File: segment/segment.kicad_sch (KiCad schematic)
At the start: 23 parts, among them J1 Voltage Taps In [1-13], J2 Thermistors In [1-12], J3 Thermistors In [13-24], J4 Voltage Taps Out [1-13], J5 Thermistors Out [1-12], J6 Thermistors Out [13-24]

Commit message: feat(segment): add sheet info
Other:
- company: (none) -> SUFST
- title: (none) -> BMS Segment Connector
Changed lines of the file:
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@@
 (kicad_sch (version 20211123) (generator eeschema)
   (paper "A4")
+  (title_block
+    (title "BMS Segment Connector")
+    (date "2022-12-02")
+    (rev "1.0.0")
+    (company "SUFST")
+    (comment 1 "STAG 9")
+    (comment 2 "Tim Brewis")
+  )
   (junction (at 43.815 147.32) (diameter 0) (color 0 0 0 0)
   )

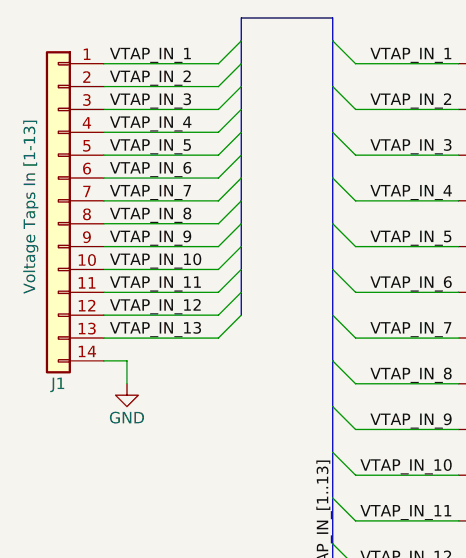
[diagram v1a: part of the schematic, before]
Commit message: feat(segment): re-do layout to reduce board width
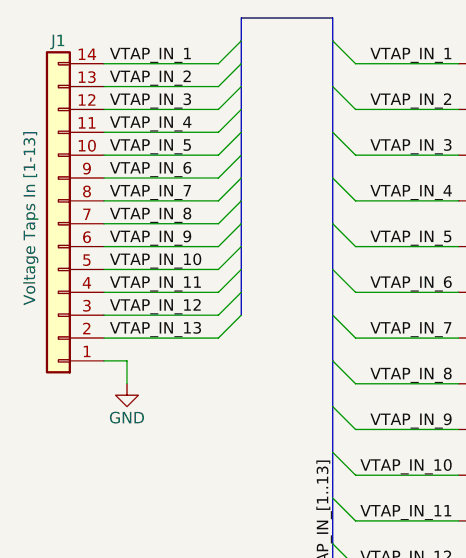
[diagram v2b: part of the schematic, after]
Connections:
- net GND: now also J1.1 (Pin_1); no longer J1.14 (Pin_14)
- net VTAP_IN_1: now also J1.14 (Pin_14); no longer J1.1 (Pin_1)
- net VTAP_IN_10: now also J1.5 (Pin_5); no longer J1.10 (Pin_10)
- net VTAP_IN_11: now also J1.4 (Pin_4); no longer J1.11 (Pin_11)
- net VTAP_IN_12: now also J1.3 (Pin_3); no longer J1.12 (Pin_12)
- net VTAP_IN_13: now also J1.2 (Pin_2); no longer J1.13 (Pin_13)
- net VTAP_IN_2: now also J1.13 (Pin_13); no longer J1.2 (Pin_2)
- net VTAP_IN_3: now also J1.12 (Pin_12); no longer J1.3 (Pin_3)
- net VTAP_IN_4: now also J1.11 (Pin_11); no longer J1.4 (Pin_4)
- net VTAP_IN_5: now also J1.10 (Pin_10); no longer J1.5 (Pin_5)
- net VTAP_IN_6: now also J1.9 (Pin_9); no longer J1.6 (Pin_6)
- net VTAP_IN_7: now also J1.8 (Pin_8); no longer J1.7 (Pin_7)
- net VTAP_IN_8: now also J1.7 (Pin_7); no longer J1.8 (Pin_8)
- net VTAP_IN_9: now also J1.6 (Pin_6); no longer J1.9 (Pin_9)
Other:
- title: BMS Segment Connector -> Segment PCB
- moved on the sheet: J1
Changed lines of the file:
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@@
   (paper "A4")
   (title_block
-    (title "BMS Segment Connector")
-    (date "2022-12-02")
-    (rev "1.0.0")
+    (title "Segment PCB")
+    (date "2022-12-03")
+    (rev "1.0.1")
     (company "SUFST")
     (comment 1 "STAG 9")
@@
     )
   )
-  (symbol (lib_id "Connector_Generic:Conn_01x14") (at 22.225 40.64 0) (mirror y) (unit 1)
+  (symbol (lib_id "Connector_Generic:Conn_01x14") (at 22.225 43.18 180) (unit 1)
     (in_bom yes) (on_board yes)
-    (property "Reference" "J1" (id 0) (at 22.225 60.96 0))
-    (property "Value" "Voltage Taps In [1-13]" (id 1) (at 19.05 41.275 90))
-    (property "Footprint" "Connector_Molex:Molex_Micro-Fit_3.0_43045-1400_2x07_P3.00mm_Horizontal" (id 2) (at 22.225 40.64 0)
+    (property "Reference" "J1" (id 0) (at 22.225 22.86 0))
+    (property "Value" "Voltage Taps In [1-13]" (id 1) (at 19.05 42.545 90))
+    (property "Footprint" "Connector_Molex:Molex_Micro-Fit_3.0_43045-1400_2x07_P3.00mm_Horizontal" (id 2) (at 22.225 43.18 0)
       (effects (font (size 1.27 1.27)) hide)
     )
-    (property "Datasheet" "https://www.molex.com/molex/products/part-detail/pcb_headers/0430451400" (id 3) (at 22.225 40.64 0)
+    (property "Datasheet" "https://www.molex.com/molex/products/part-detail/pcb_headers/0430451400" (id 3) (at 22.225 43.18 0)
       (effects (font (size 1.27 1.27)) hide)
     )

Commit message: Merge "new-dash" into "Dash" to clean up monorepo (#140)
* docs(bspd): add some more explanatory comments (#51)

* fix(vcu): drive output optocoupler signals at 12V instead of 3.3V (#57)

* feat(vcu): 12V DRS servo control (#58)

* feat(vcu): remove old DRS from schematic

* chore(vcu): remove old DRS from layout

* feat(vcu): add op-amp buffers to analogue input stage (#59)

* feat(vcu): add CMOS buffers to digital I/O interfaces (#60)

* feat(vcu): layout for v1.2.0 (#62)

* feat(vcu): layout for v1.2.0

* fix(vcu): remove accidental extra label on silkscreen

* fix(vcu): update incorrect silkscreen pin label

* release(vcu): v1.2.0 (#64)

* release(vcu): v1.2.0

* chore(vcu): add dimensions to layout

* fix(latching): corrected latching behaviour (#75)

* fix(latching): corrected latching behaviour

* chore(latching): rename files

* docs(latching): improve annotations

* fix(vcu): improve safety of input stages (#77)

* feat(vcu): pull down digital inputs

* feat(vcu): add filters and pulldown to analogue inputs

* feat(latching): revised layout for fixed latching logic (#76)

feat(latching): revised layout for new latching logic

* release(latching): v1.1.0 (#78)

* docs(latching): add some final comments

* release(latching): v1.1.0

* feat(hvs): add fusing and adjust resistor values (#79)

* feat(hvs): add fusing to HV input

* feat(hvs): round the board edges

* feat(hvs): minor silkscreen adjustments

* feat(hvs): add silkscreen labels for connectors

* feat(hvs): downsize precharge relay contact wetting resistor

* feat(hvs): add project name and version to silkscreen

* feat(hvs): add wek pull downs to logic inputs

* feat(hvs): add fuse to TS side 12V

* fix(hvs): add missing power flag

* release(hvs): v1.1.0 (#81)

* feat(hvs): add dimensions to layout

* release(hvs): v1.1.0

* fix(bspd): improve layout and fix connection issues (#74)

* fix(bspd): increase low SCS threshold

* fix(bspd): add missing IC power connec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
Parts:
- H1, H2, H3, H4: footprint MountingHole:MountingHole_3.2mm_M3 -> MountingHole:MountingHole_4.3mm_M4
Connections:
- net GND: now also J2.13 (Pin_13), J2.14 (Pin_14), J2.15 (Pin_15), J2.16 (Pin_16), J2.17 (Pin_17), J2.18 (Pin_18), J2.19 (Pin_19), J2.20 (Pin_20), J2.21 (Pin_21), J2.22 (Pin_22), J2.23 (Pin_23), J2.24 (Pin_24), J3.13 (Pin_13), J3.14 (Pin_14), J3.15 (Pin_15), J3.16 (Pin_16), J3.17 (Pin_17), J3.18 (Pin_18), J3.19 (Pin_19), J3.20 (Pin_20), J3.21 (Pin_21), J3.22 (Pin_22), J3.23 (Pin_23), J3.24 (Pin_24); no longer J1.1 (Pin_1), J2.1 (Pin_1), J2.10 (Pin_10), J2.11 (Pin_11), J2.12 (Pin_12), J2.2 (Pin_2), J2.3 (Pin_3), J2.4 (Pin_4), J2.5 (Pin_5), J2.6 (Pin_6), J2.7 (Pin_7), J2.8 (Pin_8), J2.9 (Pin_9), J3.1 (Pin_1), J3.10 (Pin_10), J3.11 (Pin_11), J3.12 (Pin_12), J3.2 (Pin_2), J3.3 (Pin_3), J3.4 (Pin_4), J3.5 (Pin_5), J3.6 (Pin_6), J3.7 (Pin_7), J3.8 (Pin_8), J3.9 (Pin_9), J4.14 (Pin_14)
- net THERM_1: now also J2.12 (Pin_12), J5.12 (Pin_12); no longer J2.24 (Pin_24), J5.1 (Pin_1)
- net THERM_10: now also J2.3 (Pin_3), J5.3 (Pin_3); no longer J2.15 (Pin_15), J5.10 (Pin_10)
- net THERM_11: now also J2.2 (Pin_2), J5.2 (Pin_2); no longer J2.14 (Pin_14), J5.11 (Pin_11)
- net THERM_12: now also J2.1 (Pin_1), J5.1 (Pin_1); no longer J2.13 (Pin_13), J5.12 (Pin_12)
- net THERM_13: now also J3.12 (Pin_12), J6.7 (Pin_7); no longer J3.24 (Pin_24), J6.1 (Pin_1)
- net THERM_14: now also J3.11 (Pin_11), J6.6 (Pin_6); no longer J3.23 (Pin_23), J6.2 (Pin_2)
- net THERM_15: now also J3.10 (Pin_10), J6.5 (Pin_5); no longer J3.22 (Pin_22), J6.3 (Pin_3)
- net THERM_16: now also J3.9 (Pin_9); no longer J3.21 (Pin_21)
- net THERM_17: now also J3.8 (Pin_8), J6.3 (Pin_3); no longer J3.20 (Pin_20), J6.5 (Pin_5)
- net THERM_18: now also J3.7 (Pin_7), J6.2 (Pin_2); no longer J3.19 (Pin_19), J6.6 (Pin_6)
- net THERM_19: now also J3.6 (Pin_6), J6.1 (Pin_1); no longer J3.18 (Pin_18), J6.7 (Pin_7)
- net THERM_2: now also J2.11 (Pin_11), J5.11 (Pin_11); no longer J2.23 (Pin_23), J5.2 (Pin_2)
- net THERM_20: now also J3.5 (Pin_5), J6.12 (Pin_12); no longer J3.17 (Pin_17), J6.8 (Pin_8)
- net THERM_21: now also J3.4 (Pin_4), J6.11 (Pin_11); no longer J3.16 (Pin_16), J6.9 (Pin_9)
- net THERM_22: now also J3.3 (Pin_3); no longer J3.15 (Pin_15)
- net THERM_23: now also J3.2 (Pin_2), J6.9 (Pin_9); no longer J3.14 (Pin_14), J6.11 (Pin_11)
- net THERM_24: now also J3.1 (Pin_1), J6.8 (Pin_8); no longer J3.13 (Pin_13), J6.12 (Pin_12)
- net THERM_3: now also J2.10 (Pin_10), J5.10 (Pin_10); no longer J2.22 (Pin_22), J5.3 (Pin_3)
- net THERM_4: now also J2.9 (Pin_9), J5.9 (Pin_9); no longer J2.21 (Pin_21), J5.4 (Pin_4)
- net THERM_5: now also J2.8 (Pin_8), J5.8 (Pin_8); no longer J2.20 (Pin_20), J5.5 (Pin_5)
- net THERM_6: now also J2.7 (Pin_7), J5.7 (Pin_7); no longer J2.19 (Pin_19), J5.6 (Pin_6)
- net THERM_7: now also J2.6 (Pin_6), J5.6 (Pin_6); no longer J2.18 (Pin_18), J5.7 (Pin_7)
- net THERM_8: now also J2.5 (Pin_5), J5.5 (Pin_5); no longer J2.17 (Pin_17), J5.8 (Pin_8)
- net THERM_9: now also J2.4 (Pin_4), J5.4 (Pin_4); no longer J2.16 (Pin_16), J5.9 (Pin_9)
- net VTAP_IN_1: now also J1.8 (Pin_8); no longer J1.14 (Pin_14)
- net VTAP_IN_10: now also J1.4 (Pin_4); no longer J1.5 (Pin_5)
- net VTAP_IN_11: now also J1.5 (Pin_5); no longer J1.4 (Pin_4)
- net VTAP_IN_12: now also J1.6 (Pin_6); no longer J1.3 (Pin_3)
- net VTAP_IN_13: now also J1.7 (Pin_7); no longer J1.2 (Pin_2)
- net VTAP_IN_2: now also J1.9 (Pin_9); no longer J1.13 (Pin_13)
- net VTAP_IN_3: now also J1.10 (Pin_10); no longer J1.12 (Pin_12)
- net VTAP_IN_5: now also J1.12 (Pin_12); no longer J1.10 (Pin_10)
- net VTAP_IN_6: now also J1.13 (Pin_13); no longer J1.9 (Pin_9)
- net VTAP_IN_7: now also J1.14 (Pin_14); no longer J1.8 (Pin_8)
- net VTAP_IN_8: now also J1.2 (Pin_2); no longer J1.7 (Pin_7)
- net VTAP_IN_9: now also J1.3 (Pin_3); no longer J1.6 (Pin_6)
- no-connect marks 0 -> 2
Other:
- note removed: "Grounds on pins 1 to 12 so that signals can be on the inside of the PCB, simpler routing"
